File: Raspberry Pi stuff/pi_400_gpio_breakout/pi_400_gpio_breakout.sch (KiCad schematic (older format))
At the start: 13 parts, among them J1 I2C, J2 RPI_IN, J3 SPI_I2S, J4 QWIIC1, J5 RPI_IN, J6 QWIIC2

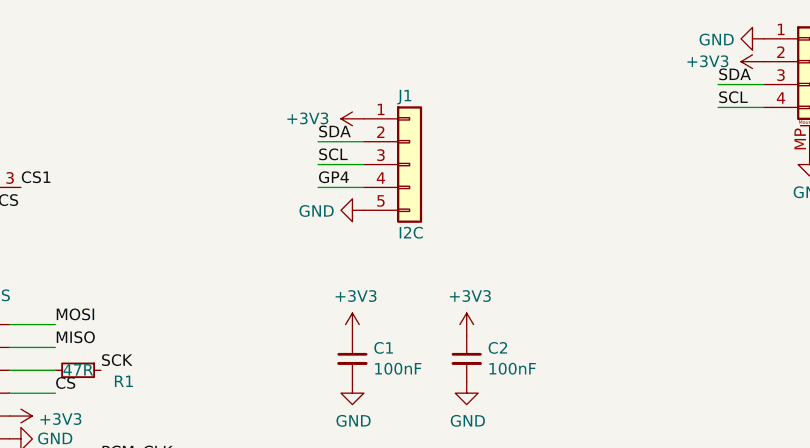
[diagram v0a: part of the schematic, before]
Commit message: Pi 400 GPIO breakout v2. Adding this in part because I'll try to re-route it now and might fail at that, so will need to fall back to the previous version.
Force pushed later on  - forgot to regenerate zones.
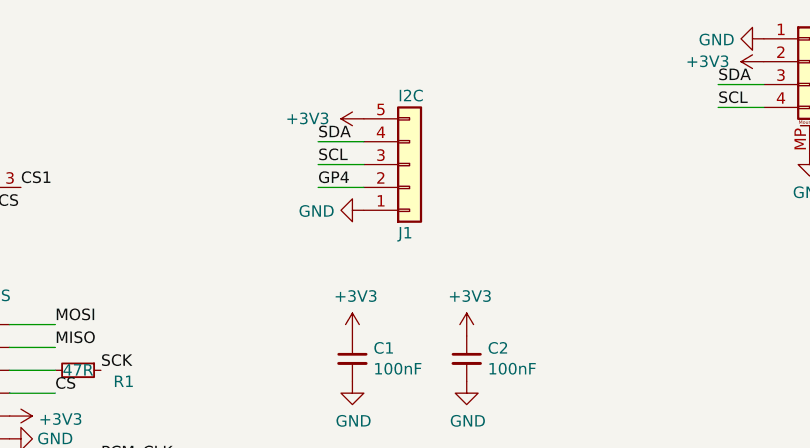
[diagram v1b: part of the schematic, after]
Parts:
- J1: footprint Connector_PinHeader_2.54mm:PinHeader_1x05_P2.54mm_Vertical -> Connector_PinSocket_2.54mm:PinSocket_1x05_P2.54mm_Horizontal
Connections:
- net +3V3: now also J1.5 (Pin_5); no longer J1.1 (Pin_1)
- net GND: now also J1.1 (Pin_1); no longer J1.5 (Pin_5)
- net GP4: now also J1.2 (Pin_2); no longer J1.4 (Pin_4)
- net SDA: now also J1.4 (Pin_4); no longer J1.2 (Pin_2)
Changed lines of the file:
@@
 F 0 "J1" H 6000 1600 50  0000 L CNN
 F 1 "I2C" H 6000 1000 50  0000 L CNN
-F 2 "Connector_PinHeader_2.54mm:PinHeader_1x05_P2.54mm_Vertical" H 6050 1300 50  0001 C CNN
+F 2 "Connector_PinSocket_2.54mm:PinSocket_1x05_P2.54mm_Horizontal" H 6050 1300 50  0001 C CNN
 F 3 "~" H 6050 1300 50  0001 C CNN
 	1    6050 1300
-	1    0    0    -1
+	1    0    0    1
 $EndComp
 $Comp
